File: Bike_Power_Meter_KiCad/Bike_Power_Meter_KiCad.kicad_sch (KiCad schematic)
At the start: 15 parts

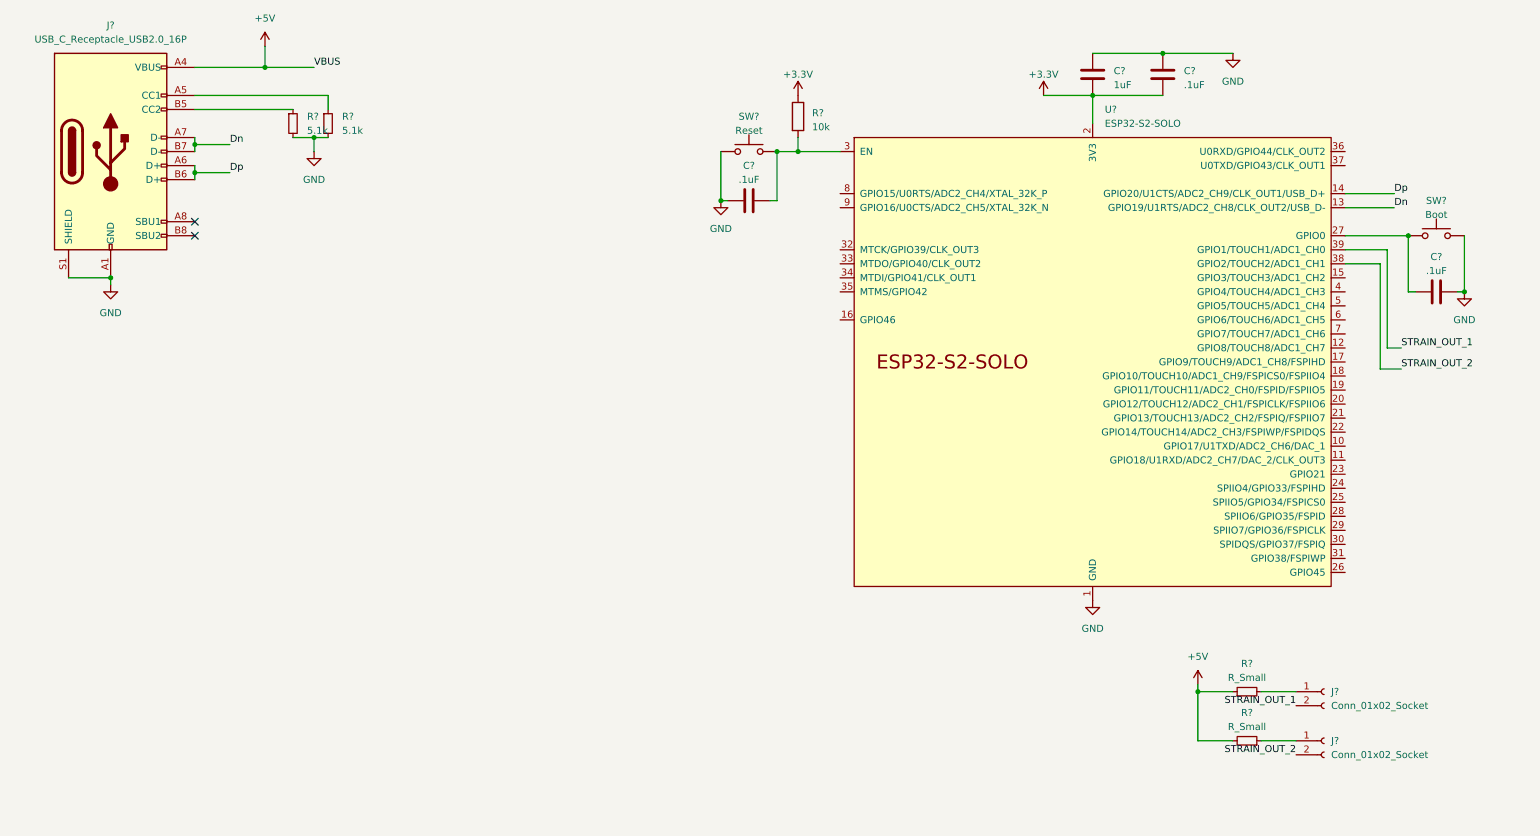
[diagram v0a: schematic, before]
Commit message: schematic done. Need to consider: adc, battery, imu interrupts
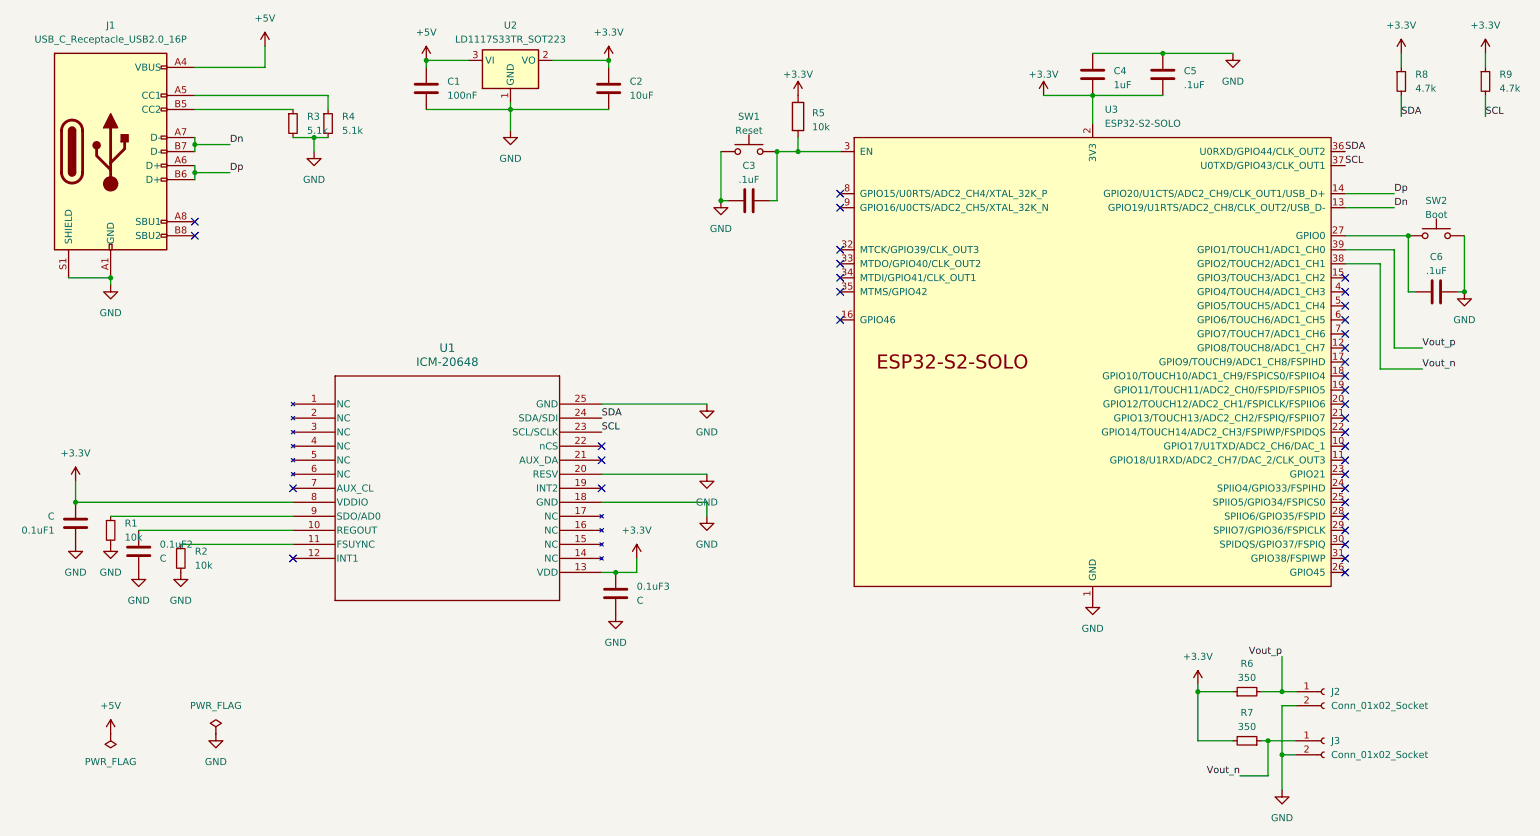
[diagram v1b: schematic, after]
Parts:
- added 0.1uF1, 0.1uF2, 0.1uF3: C, symbol Device:C
- added C1: 100nF, symbol Device:C
- added C2: 10uF, symbol Device:C
- added R1, R2: 10k, symbol Device:R_Small
- added R8, R9: 4.7k, symbol Device:R_Small
- added U1: ICM-20648, QFN24_3X3X0P9_IVS, symbol Bike_Power_Meter_Import:ICM-20648
- added U2: LD1117S33TR_SOT223, Package_TO_SOT_SMD:SOT-223-3_TabPin2, symbol Regulator_Linear:LD1117S33TR_SOT223
- R6, R7: renamed from R?; value R_Small -> 350
- gave numbers to parts that had none: 13
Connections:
- net +3.3V: now also R6.1, R7.2, 0.1uF1.2, 0.1uF3.1, C2.1, R8.1, R9.1, U1.13 (VDD), U1.8 (VDDIO), U2.2 (VO)
- net +5V: now also C1.1, U2.3 (VI); no longer R6.1, R7.2
- net GND: now also J2.2 (Pin_2), J3.2 (Pin_2), 0.1uF1.1, 0.1uF2.2, 0.1uF3.2, C1.2, C2.2, R1.2, R2.2, U1.18 (GND), U1.20 (RESV), U1.25 (GND), U2.1 (GND)
- net Vout_n: now reaches J3.1 (Pin_1), R7.1
- net Vout_n: now also U3.38 (GPIO2/TOUCH2/ADC1_CH1)
- net Vout_p: now reaches J2.1 (Pin_1), R6.2
- net Vout_p: now also U3.39 (GPIO1/TOUCH1/ADC1_CH0)
- net SDA: now reaches U3.36 (U0RXD/GPIO44/CLK_OUT2)
- net SDA: now also R8.2, U1.24 (SDA/SDI)
- net SCL: now reaches U3.37 (U0TXD/GPIO43/CLK_OUT1)
- net SCL: now also R9.2, U1.23 (SCL/SCLK)
- removed net STRAIN_OUT_1: J2.2 (Pin_2), U3.39 (GPIO1/TOUCH1/ADC1_CH0)
- removed net STRAIN_OUT_2: J3.2 (Pin_2), U3.38 (GPIO2/TOUCH2/ADC1_CH1)
- new net: R2.1, U1.11 (FSUYNC)
- new net: 0.1uF2.1, U1.10 (REGOUT)
- new net: R1.1, U1.9 (SDO/AD0)
- no-connect marks 2 -> 36

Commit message: also need to think about indicator LEDs
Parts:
- renumbered 0.1uF3 to 0.1uF
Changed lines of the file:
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@@
 		(dnp no)
 		(fields_autoplaced yes)
-		(property "Reference" "0.1uF3"
+		(property "Reference" "0.1uF"
 			(at 123.19 116.8399 0)
 			(effects
@@
 			(project ""
 				(path "/edabeeff-0186-4a5a-99ed-27c2963ab15f"
-					(reference "0.1uF3")
+					(reference "0.1uF")
 					(unit 1)
 				)
